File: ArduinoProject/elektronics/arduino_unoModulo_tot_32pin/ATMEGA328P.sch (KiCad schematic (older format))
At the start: 8 parts, among them SW601 RESET_SWITCH, U601 ATMEGA328P-MU20, X601 CSTCE16MOV53-R0

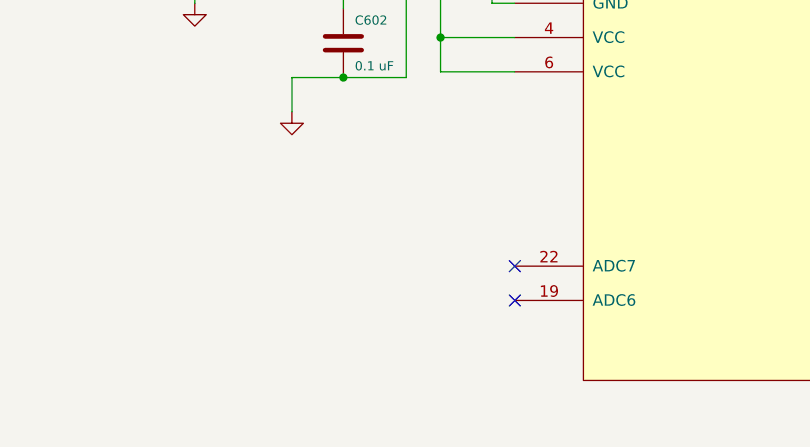
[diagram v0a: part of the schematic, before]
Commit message: analog pins added
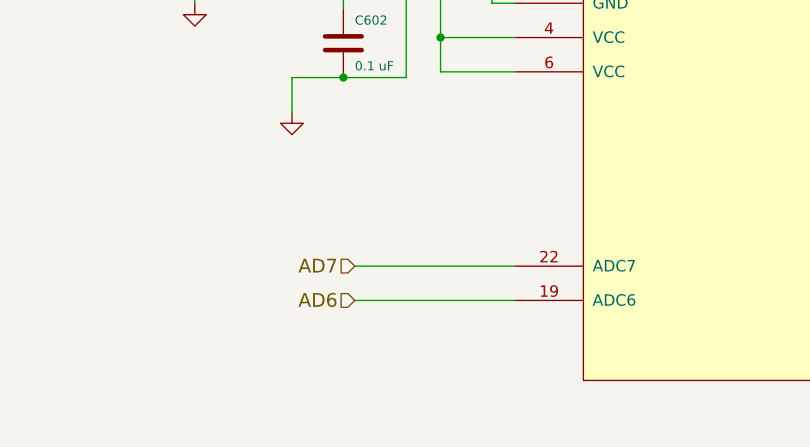
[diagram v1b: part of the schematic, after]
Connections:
- net AD6: now reaches U601.19 (ADC6)
- net AD7: now reaches U601.22 (ADC7)
- no-connect marks 2 -> 0
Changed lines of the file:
@@
-	1    0    0    -1
-$EndComp
-$Comp
-L ATMEGA328P-MU20 U601
-U 1 1 5A9E5226
-P 7050 3750
-F 0 "U601" H 8000 1150 60  0000 C CNN
-F 1 "ATMEGA328P-MU20" H 7050 6300 60  0000 C CNN
-F 2 "ATMEGA328P-AN:QFP80P900X900X120-32N" H 6950 5250 60  0001 C CNN
-F 3 "" H 6950 5250 60  0000 C CNN
-	1    7050 3750
 	1    0    0    -1
 $EndComp
@@
 	5850 4050 5375 4050
 Connection ~ 5375 4400
-NoConn ~ 5850 5700
-NoConn ~ 5850 5850
 $Comp
 L +5V #PWR032
@@
 Wire Wire Line
 	4900 750  4050 750
+$Comp
+L ATMEGA328P-MU20 U601
+U 1 1 5A9E5226
+P 7050 3750
+F 0 "U601" H 8000 1150 60  0000 C CNN
+F 1 "ATMEGA328P-MU20" H 7050 6300 60  0000 C CNN
+F 2 "ATMEGA328P-AN:QFP80P900X900X120-32N" H 6950 5250 60  0001 C CNN
+F 3 "" H 6950 5250 60  0000 C CNN
+	1    7050 3750
+	1    0    0    -1
+$EndComp
+Wire Wire Line
+	5850 5700 5150 5700
+Wire Wire Line
+	5850 5850 5150 5850
+Text HLabel 5150 5850 0    60   Input ~ 0
+AD6
+Text HLabel 5150 5700 0    60   Input ~ 0
+AD7
 $EndSCHEMATC

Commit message: arduino routed
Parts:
- SW601: footprint Buttons_Switches_Keyboard:SW_Cherry_MX1A_1.00u_Plate -> 4-1437565-1:FSM-SWITCH
- U601: footprint ATMEGA328P-AN:QFP80P900X900X120-32N -> ATMEGA328P-AU:QFP80P900X900X120-32N
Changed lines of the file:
@@
 F 0 "SW601" V 3250 2275 60  0000 C CNN
 F 1 "RESET_SWITCH" V 3550 2525 60  0000 C CNN
-F 2 "Buttons_Switches_Keyboard:SW_Cherry_MX1A_1.00u_Plate" H 3400 1975 60  0001 C CNN
+F 2 "4-1437565-1:FSM-SWITCH" H 3400 1975 60  0001 C CNN
 F 3 "http://industrial.panasonic.com/www-data/pdf/ATK0000/ATK0000CE28.pdf" H 3400 1975 60  0001 C CNN
 F 4 "SWITCH TACTILE SPST-NO 0.02A 15V" H 3400 1975 60  0001 C CNN "Characteristics"
@@
 F 0 "U601" H 8000 1150 60  0000 C CNN
 F 1 "ATMEGA328P-MU20" H 7050 6300 60  0000 C CNN
-F 2 "ATMEGA328P-AN:QFP80P900X900X120-32N" H 6950 5250 60  0001 C CNN
+F 2 "ATMEGA328P-AU:QFP80P900X900X120-32N" H 6950 5250 60  0001 C CNN
 F 3 "" H 6950 5250 60  0000 C CNN
 	1    7050 3750

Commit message: new components
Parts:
- removed R602: 1M, Resistors_SMD:R_0805, symbol R
- removed X601: CSTCE16MOV53-R0, CSTCE16M0V53ZW-R0:CSTE_G_A, symbol CERAMIC_RESONATOR
- added C603, C604: 22p, Capacitors_SMD:C_0805, symbol C
- added Y601: Crystal, MCRSD16000F183000RR:HC%2f49US-(AT49)_1, symbol Crystal
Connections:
- net GND: now also C603.1, C604.1
- net at U601.8 (PB7(XTAL2/TOSC2)): now also C603.2, Y601.1
- net at U601.7 (PB6(XTAL1/TOSC1)): now also C604.2, Y601.2
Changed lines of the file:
@@
 Comment4 ""
 $EndDescr
-Wire Wire Line
-	5650 2050 5650 2400
-Connection ~ 5650 2050
-Wire Wire Line
-	5650 2700 5650 3050
-Connection ~ 5650 3050
 Text HLabel 4150 3750 0    40   Input ~ 0
 AREF
@@
 Wire Wire Line
 	3200 950  3200 1500
-$Comp
-L CERAMIC_RESONATOR X601
-U 1 1 5614A1DB
-P 5250 2550
-F 0 "X601" V 5325 2450 50  0000 R CNN
-F 1 "CSTCE16MOV53-R0" V 5175 2450 40  0000 R CNN
-F 2 "CSTCE16M0V53ZW-R0:CSTE_G_A" H 5250 2550 60  0000 C CNN
-F 3 "http://www.murata.com/~/media/webrenewal/support/library/catalog/products/timingdevice/ceralock/p16e.ashx" H 5250 2550 60  0001 C CNN
-F 4 "CER RESONATOR 16.0MHZ SMD" H 5250 2550 60  0001 C CNN "Characteristics"
-F 5 "ATMEGA328P Oscillator" H 5250 2550 60  0001 C CNN "Description"
-F 6 "Murata" H 5250 2550 60  0001 C CNN "MFN"
-F 7 "CSTCE16M0V53-R0" H 5250 2550 60  0001 C CNN "MFP"
-F 8 "SMD" H 5250 2550 60  0001 C CNN "Package ID"
-F 9 "ANY" H 5250 2550 60  0001 C CNN "Source"
-F 10 "Y" H 5250 2550 60  0001 C CNN "Critical"
-F 11 "328P_Sub" H 5250 2550 60  0001 C CNN "Subsystem"
-F 12 "~" H 5250 2550 60  0001 C CNN "Notes"
-	1    5250 2550
-	0    1    1    0
-$EndComp
-Wire Wire Line
-	5300 2050 5850 2050
-Wire Wire Line
-	5300 2050 5300 2150
-Wire Wire Line
-	5300 2950 5300 3050
-Wire Wire Line
-	5300 3050 5850 3050
-Wire Wire Line
-	5050 2550 4750 2550
-Wire Wire Line
-	4750 2550 4750 2900
+Wire Wire Line
+	4625 2050 5850 2050
+Wire Wire Line
+	5300 2050 5300 2425
+Wire Wire Line
+	5300 2725 5300 3050
+Wire Wire Line
+	4600 3050 5850 3050
 Text Notes 6150 1050 0    40   ~ 0
 Atmel Appnote: AVR042 - AVR Hardware Design Considerations\nhttp://www.atmel.com/Images/Atmel-2521-AVR-Hardware-Design-Considerations_ApplicationNote_AVR042.pdf\n\nRefer to this for PCB layout information
@@
 	-1   0    0    1
 $EndComp
-$Comp
-L R R602
-U 1 1 5615BCD3
-P 5650 2550
-F 0 "R602" H 5725 2500 40  0000 L CNN
-F 1 "1M" V 5650 2550 40  0000 C CNN
-F 2 "Resistors_SMD:R_0805" V 5580 2550 30  0001 C CNN
-F 3 "http://www.vishay.com/docs/20035/dcrcwe3.pdf" H 5650 2550 30  0001 C CNN
-F 4 "RES SMD 1M OHM 1% 1/8W 0805" H 5650 2550 60  0001 C CNN "Characteristics"
-F 5 "ATMEGA328P Xtal 1M Feedback Resistor" H 5650 2550 60  0001 C CNN "Description"
-F 6 "Vishay" H 5650 2550 60  0001 C CNN "MFN"
-F 7 "CRCW08051M00FKEA" H 5650 2550 60  0001 C CNN "MFP"
-F 8 "SMD_0805" H 5650 2550 60  0001 C CNN "Package ID"
-F 9 "ANY" H 5650 2550 60  0001 C CNN "Source"
-F 10 "N" H 5650 2550 60  0001 C CNN "Critical"
-F 11 "328P_Sub" H 5650 2550 60  0001 C CNN "Subsystem"
-F 12 "~" H 5650 2550 60  0001 C CNN "Notes"
-	1    5650 2550
-	1    0    0    -1
-$EndComp
 Wire Wire Line
 	3500 1650 3500 1775
@@
 $Comp
 L GND #PWR029
-U 1 1 56207870
-P 4750 2900
-F 0 "#PWR029" H 4750 2900 30  0001 C CNN
-F 1 "GND" H 4750 2830 30  0001 C CNN
-F 2 "~" H 4750 2900 60  0000 C CNN
-F 3 "~" H 4750 2900 60  0000 C CNN
-F 4 "ANY" H 4750 2900 60  0001 C CNN "Source"
-F 5 "N" H 4750 2900 60  0001 C CNN "Critical"
-F 6 "~" H 4750 2900 60  0001 C CNN "Notes"
-	1    4750 2900
-	1    0    0    -1
-$EndComp
-$Comp
-L GND #PWR030
 U 1 1 562079B8
 P 3400 2425
-F 0 "#PWR030" H 3400 2425 30  0001 C CNN
+F 0 "#PWR029" H 3400 2425 30  0001 C CNN
 F 1 "GND" H 3400 2355 30  0001 C CNN
 F 2 "~" H 3400 2425 60  0000 C CNN
@@
 $EndComp
 $Comp
-L GND #PWR031
+L GND #PWR030
 U 1 1 56208C49
 P 4350 1100
-F 0 "#PWR031" H 4350 1100 30  0001 C CNN
+F 0 "#PWR030" H 4350 1100 30  0001 C CNN
 F 1 "GND" H 4350 1030 30  0001 C CNN
 F 2 "~" H 4350 1100 60  0000 C CNN
@@
 Connection ~ 5375 4400
 $Comp
-L +5V #PWR032
+L +5V #PWR031
 U 1 1 5A9E5CDE
 P 4925 4450
-F 0 "#PWR032" H 4925 4300 50  0001 C CNN
+F 0 "#PWR031" H 4925 4300 50  0001 C CNN
 F 1 "+5V" H 4925 4590 50  0000 C CNN
 F 2 "" H 4925 4450 50  0001 C CNN
@@
 	4925 4475 4925 4450
 $Comp
-L +5V #PWR033
+L +5V #PWR032
 U 1 1 5A9E5E9A
 P 4900 650
-F 0 "#PWR033" H 4900 500 50  0001 C CNN
+F 0 "#PWR032" H 4900 500 50  0001 C CNN
 F 1 "+5V" H 4900 790 50  0000 C CNN
 F 2 "" H 4900 650 50  0001 C CNN
@@
 Text HLabel 5150 5700 0    60   Input ~ 0
 AD7
+$Comp
+L Crystal Y601
+U 1 1 5AA8FA43
+P 5300 2575
+F 0 "Y601" H 5300 2725 50  0000 C CNN
+F 1 "Crystal" H 5300 2425 50  0000 C CNN
+F 2 "MCRSD16000F183000RR:HC%2f49US-(AT49)_1" H 5300 2575 50  0001 C CNN
+F 3 "" H 5300 2575 50  0001 C CNN
+	1    5300 2575
+	0    1    1    0
+$EndComp
+Connection ~ 5300 2050
+$Comp
+L C C603
+U 1 1 5AA8FDA4
+P 4475 2050
+F 0 "C603" H 4500 2150 50  0000 L CNN
+F 1 "22p" H 4500 1950 50  0000 L CNN
+F 2 "Capacitors_SMD:C_0805" H 4513 1900 50  0001 C CNN
+F 3 "" H 4475 2050 50  0001 C CNN
+	1    4475 2050
+	0    -1   -1   0
+$EndComp
+Wire Wire Line
+	4325 2050 4325 2250
+$Comp
+L GND #PWR033
+U 1 1 5AA8FEAC
+P 4325 2250
+F 0 "#PWR033" H 4325 2000 50  0001 C CNN
+F 1 "GND" H 4325 2100 50  0000 C CNN
+F 2 "" H 4325 2250 50  0001 C CNN
+F 3 "" H 4325 2250 50  0001 C CNN
+	1    4325 2250
+	1    0    0    -1
+$EndComp
+Connection ~ 5300 3050
+$Comp
+L C C604
+U 1 1 5AA8FFE3
+P 4450 3050
+F 0 "C604" H 4475 3150 50  0000 L CNN
+F 1 "22p" H 4475 2950 50  0000 L CNN
+F 2 "Capacitors_SMD:C_0805" H 4488 2900 50  0001 C CNN
+F 3 "" H 4450 3050 50  0001 C CNN
+	1    4450 3050
+	0    -1   -1   0
+$EndComp
+$Comp
+L GND #PWR034
+U 1 1 5AA90121
+P 4300 3150
+F 0 "#PWR034" H 4300 2900 50  0001 C CNN
+F 1 "GND" H 4300 3000 50  0000 C CNN
+F 2 "" H 4300 3150 50  0001 C CNN
+F 3 "" H 4300 3150 50  0001 C CNN
+	1    4300 3150
+	1    0    0    -1
+$EndComp
+Wire Wire Line
+	4300 3050 4300 3150
 $EndSCHEMATC
